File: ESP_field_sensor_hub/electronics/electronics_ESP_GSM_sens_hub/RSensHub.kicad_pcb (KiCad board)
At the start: 2 copper layers, 25 parts, among them J1 RJ45_Shielded, J2 RJ45_Shielded, J4 Conn_01x04_Female, Q1 IRF3205, Q2 IRF3205, Q3 IRF3205, Q4 IRF3205, Q5 IRF3205, Q6 IRF3205, U1 MAX48_module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

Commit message: Previous
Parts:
- added ANT: , myComponents:GNSSantennaVertical, F.Cu at (209.0, 26.7)
- added U4: SIM7000G_DEVBoard, myComponents:sim7000G_dev_board, F.Cu at (183.5, 45.7)
- moved U3 91.1 mm to (187.3, 106.0), turned to 90 degrees

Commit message: worked on sens hub PCB
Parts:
- removed ANT: , myComponents:GNSSantennaVertical
- added AE1: Antenna, myComponents:GNSSantennaVertical, F.Cu at (241.4, 30.5)
- added C2: 1000u16V, myComponents:CAP_Radial_D10.0mm_P5.00mm, F.Cu at (198.8, 38.7)
- added D1: LED, myComponents:LED_small_D3.0mm, F.Cu at (263.5, 50.2)
- added D2: LED, myComponents:LED_small_D3.0mm, F.Cu at (263.5, 60.3)
- added D4: LED, myComponents:LED_small_D3.0mm, F.Cu at (263.5, 65.4)
- added D5: LED, myComponents:LED_small_D3.0mm, F.Cu at (263.5, 70.5)
- added D6: LED, myComponents:LED_small_D3.0mm, F.Cu at (263.5, 45.1)
- added D7: LED, myComponents:LED_small_D3.0mm, F.Cu at (263.5, 55.2)
- added J6: Conn_01x04_Female, myComponents:TerminalBlockRemovablex4, F.Cu at (250.2, 90.8)
- added JP2: SolderJumper_2_Open, Jumper:SolderJumper-2_P1.3mm_Open_RoundedPad1.0x1.5mm, F.Cu at (217.8, 50.2)
- added JP3: Jumper_2_Bridged, myComponents:jumperx2_P2.54mm_widePads, F.Cu at (263.5, 77.5)
- added JP4: Jumper_2_Bridged, myComponents:jumperx2_P2.54mm_widePads, F.Cu at (263.5, 40.6)
- added JP5: Jumper_2_Bridged, myComponents:jumperx2_P2.54mm_widePads, F.Cu at (48.8, 16.8)
- added JP6: Jumper_2_Bridged, myComponents:jumperx2_P2.54mm_widePads, F.Cu at (52.3, 16.8)
- added R17: R, myComponents:resistor0.25,9mm, F.Cu at (248.3, 70.5)
- added R18: R, myComponents:resistor0.25,9mm, F.Cu at (248.2, 55.2)
- moved J1 147.2 mm to (232.4, 92.7), turned to 0 degrees
- moved U1 144.5 mm to (236.9, 37.5), turned to 270 degrees
- moved Q6 129.8 mm to (43.6, 89.2)
- moved R1 126.5 mm to (248.3, 50.2)
- moved J2 125.6 mm to (214.0, 92.7), turned to 0 degrees
- moved R2 125.0 mm to (248.3, 45.1)
- moved R15 118.8 mm to (33.0, 45.7)
- moved Q5 118.6 mm to (54.0, 78.9)
- moved R14 114.6 mm to (248.3, 65.4)
- moved R13 114.3 mm to (248.3, 60.3)
- moved J4 112.5 mm to (188.6, 90.2), turned to 90 degrees
- moved R16 100.6 mm to (50.8, 35.4)
- moved R3 98.0 mm to (38.8, 31.4)
- moved R12 86.7 mm to (63.6, 45.4)
- moved R9 86.2 mm to (64.8, 3.81)
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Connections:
- J2 pad 1: GND -> Net-(J2-Pad1)
- J2 pad 2: GND -> Net-(J2-Pad1)
- R1 pad 1: Net-(D1-Pad1) -> /SIM_IN_LED
- R1 pad 2: GND -> Net-(D1-Pad2)
- R13 pad 1: Net-(D4-Pad1) -> /COM_IN_LED
- R13 pad 2: GND -> Net-(D2-Pad2)
- R14 pad 1: Net-(D5-Pad1) -> /COM_OUT_LED
- R14 pad 2: GND -> Net-(D4-Pad2)
- R2 pad 1: Net-(D2-Pad1) -> /SIM_OUT_LED
- R2 pad 2: GND -> Net-(D6-Pad2)
- U1 pad 1: /UART2_RX -> /COM_IN_LED
- U1 pad 4: /UART2_TX -> /COM_OUT_LED
- U3 pad 14: Net-(U3-Pad14) -> GND
- U3 pad 19: Net-(U3-Pad19) -> +5V
- U3 pad 20: Net-(U3-Pad20) -> GND
- U3 pad 25: Net-(U3-Pad25) -> /UART2_DRIVER
- U3 pad 26: Net-(U3-Pad26) -> GND
- U3 pad 27: Net-(U3-Pad27) -> /COM_OUT_LED
- U3 pad 28: Net-(U3-Pad28) -> /COM_IN_LED
- U3 pad 30: Net-(U3-Pad30) -> /SIM_OUT_LED
- U3 pad 31: Net-(U3-Pad31) -> /SIM_IN_LED
- U4 pad 6: /uTX_SIM7000 -> /SIM_OUT_LED
- U4 pad 8: /uRX_SIM7000 -> /SIM_IN_LED

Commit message: short circuit protection - tested on dot board, ESP control pins not connected
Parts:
- removed D1, D2, D4, D5, D6, D7: LED, myComponents:LED_small_D3.0mm
- removed J6: Conn_01x04_Female, myComponents:TerminalBlockRemovablex4
- removed Q1, Q2, Q3, Q5, Q6: IRF3205, Package_TO_SOT_THT:TO-220-3_Vertical
- removed R1, R2: R, myComponents:resistor0.25,9mm
- removed R11, R15, R3: 470R, myComponents:resistor0.25,9mm
- removed R16, R7: 10K, myComponents:resistor0.25,9mm
- added C3: 100nF, myComponents:Capker_L4.6mm_W2.0mm_P2.50mm, F.Cu at (82.9, 68.1)
- added C4: 100nF, myComponents:Capker_L4.6mm_W2.0mm_P2.50mm, F.Cu at (82.9, 64.7)
- added JP1: SolderJumper_2_Open, Jumper:SolderJumper-2_P1.3mm_Open_RoundedPad1.0x1.5mm, F.Cu at (127.1, 77.7)
- added R19: 120, myComponents:resistor0.25,9mm, F.Cu at (86.7, 111.1)
- added R20: 120, myComponents:resistor0.25,9mm, F.Cu at (129.4, 91.8)
- added R21: 120, myComponents:resistor0.25,9mm, F.Cu at (156.0, 58.4)
- added R22: R, myComponents:resistor0.25,9mm, F.Cu at (110.8, 99.0)
- added R28: 1K, myComponents:resistor0.25,9mm, F.Cu at (232.0, 74.5)
- added R29: 1K, myComponents:resistor0.25,9mm, F.Cu at (86.7, 103.0)
- added R8: R0, myComponents:resistor0.25,9mm, F.Cu at (50.6, 110.3)
- added REF**: Box190x140x70, myComponents:Box190x140x70, F.Cu at (-521.5, -19.8)
- added RN1: R_Network08, myComponents:PinHeader_1x9_P2.54mm_widePads, F.Cu at (143.3, 32.6)
- added U10: PC817, myComponents:optoCouplerDIP4, F.Cu at (233.3, 78.2)
- added U11: PC817, myComponents:optoCouplerDIP4, F.Cu at (233.3, 84.3)
- added U12: PC817, myComponents:optoCouplerDIP4, F.Cu at (233.3, 68.6)
- added U2: 5V5ADCDC, myComponents:DCDC_HCW_P715, F.Cu at (29.8, 34.9)
- added U6: MULTICOL_LED_BAR, myComponents:DIP-20_LED_BAR_DISP, F.Cu at (131.3, 32.6)
- JP5: value Jumper_2_Bridged -> RS485 terminator
- JP6: value Jumper_2_Bridged -> SolderJumper_2_Open; footprint myComponents:jumperx2_P2.54mm_widePads -> Jumper:SolderJumper-2_P1.3mm_Open_RoundedPad1.0x1.5mm
- Q4: value IRF3205 -> IRF540N; footprint Package_TO_SOT_THT:TO-220-3_Vertical -> myComponents:TO-220-3_Horizontal_TabDown_bothSides
- R12: value 10K -> 330R
- R13, R18: value R -> 330R
- R14: value R -> 1K
- R17: value R -> 100K
- moved JP6 198.9 mm to (237.1, 90.3), turned to 90 degrees
- moved JP4 183.6 mm to (82.5, 71.4), turned to 0 degrees
- moved U4 181.5 mm to (27.0, 76.3)
- moved Q4 171.7 mm to (247.1, 84.8)
- moved R12 162.1 mm to (221.8, 80.9)
- moved U1 161.4 mm to (82.6, 85.0), turned to 0 degrees
- moved R18 148.0 mm to (104.5, 91.1)
- moved AE1 117.4 mm to (124.1, 33.1), turned to 0 degrees
- moved JP2 116.2 mm to (125.4, 120.5), turned to 0 degrees
- moved C2 109.6 mm to (112.8, 106.8), turned to 0 degrees
- moved R9 106.6 mm to (62.6, 110.3)
- moved JP3 103.3 mm to (170.8, 32.1), turned to 0 degrees
- moved R6 85.4 mm to (38.5, 110.3)
- moved R10 69.9 mm to (74.7, 110.3)
- moved R5 64.5 mm to (82.3, 99.0)
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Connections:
- J1 pad 1: GND -> /SAFE_BAT_GND
- J1 pad 2: GND -> /SAFE_BAT_GND
- J1 pad 7: VBUS -> +BATT
- J1 pad 8: VBUS -> +BATT
- J2 pad 1: Net-(J2-Pad1) -> /SAFE_BAT_GND
- J2 pad 2: Net-(J2-Pad1) -> /SAFE_BAT_GND
- J2 pad 7: VBUS -> +BATT
- J2 pad 8: VBUS -> +BATT
- J4 pad 2: /V_SOLAR -> +BATT
- J4 pad 4: +BATT -> /V_SOLAR
- JP3 pad 1: Net-(D2-Pad1) -> GND
- JP3 pad 2: GND -> Net-(JP3-Pad2)
- JP4 pad 1: Net-(D1-Pad1) -> GND
- JP4 pad 2: GND -> Net-(JP4-Pad2)
- JP5 pad 2: Net-(JP5-Pad2) -> /RS485_A
- Q4 pad 1: Net-(Q3-Pad1) -> Net-(JP6-Pad2)
- Q4 pad 2: /LOAD1_SOURCE -> /SAFE_BAT_GND
- R10 pad 2: /VREAD_ENABLED -> GND
- R12 pad 1: Net-(Q3-Pad1) -> GND
- R12 pad 2: GND -> Net-(R12-Pad2)
- R13 pad 1: /COM_IN_LED -> GND
- R14 pad 1: /COM_OUT_LED -> +BATT
- R17 pad 1: VBUS -> Net-(JP6-Pad1)
- R17 pad 2: Net-(D5-Pad2) -> GND
- R18 pad 1: +5V -> +3V3
- R6 pad 2: /VREAD_ENABLED -> GND

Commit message: worked on sens hub PCB layout, mostly done, needs finishing touches
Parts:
- removed the REF** at (-521.5, -19.8)
- added D3: D, myComponents:1N41_Diode, F.Cu at (306.7, 90.8)
- added J3: Conn_01x12_Male, myComponents:PinHeader_1x12_P2.54mm_widePads, F.Cu at (340.4, 83.2)
- added REF**: M3 mechanical, myComponents:M3 mechanical, F.Cu at (363.2, 26.7)
- added REF**: M3 mechanical, myComponents:M3 mechanical, F.Cu at (304.8, 77.9)
- added REF**: M3 mechanical, myComponents:M3 mechanical, F.Cu at (404.6, 77.9)
- added RV1: R_POT, myComponents:Potentiometer_ACP_CA9-V10_Vertical_Hole, F.Cu at (379.9, 100.9)
- JP1, JP2, JP6: moved to B.Cu
- moved JP4 319.5 mm to (400.1, 35.6)
- moved R29 319.1 mm to (404.0, 68.6), turned to 180 degrees
- moved U4 314.5 mm to (339.7, 43.2)
- moved R6 311.3 mm to (348.6, 83.2)
- moved R19 296.7 mm to (379.7, 64.7), turned to 270 degrees
- moved JP5 294.6 mm to (383.5, 76.8), turned to 270 degrees
- moved U1 294.2 mm to (372.1, 32.4), turned to 270 degrees
- moved U2 290.0 mm to (312.9, 97.8), turned to 90 degrees
- moved R22 286.1 mm to (391.2, 41.9), turned to 180 degrees
- moved R10 275.0 mm to (348.6, 87.0)
- moved C4 272.7 mm to (354.4, 90.2)
- moved C3 271.7 mm to (354.3, 80.0)
- moved U6 263.8 mm to (395.0, 41.9)
- moved RN1 263.3 mm to (406.4, 44.5)
- moved U3 256.5 mm to (345.4, 78.1)
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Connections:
- J4 pad 1: GND -> +BATT
- J4 pad 2: +BATT -> GND
- R5 pad 1: +BATT -> /V_SOLAR
- R9 pad 1: /V_SOLAR -> +BATT
- U3 pad 21: Net-(U3-Pad21) -> /Vout_OFF
- U3 pad 22: Net-(U3-Pad22) -> /Vout_ON
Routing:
- net GND: track 0.00 -> 408.1 mm
- net +5V: track 0.00 -> 251.3 mm, vias 0 -> 3
- net +BATT: track 0.00 -> 206.6 mm
- net /COM_IN_LED: track 0.00 -> 143.6 mm, vias 0 -> 6
- net /SIM_IN_LED: track 0.00 -> 136.9 mm, vias 0 -> 7
- net /SIM_OUT_LED: track 0.00 -> 133.6 mm, vias 0 -> 2
- net /COM_OUT_LED: track 0.00 -> 124.9 mm, vias 0 -> 6
- net /RS485_A: track 0.00 -> 115.0 mm
- net /RS485_B: track 0.00 -> 104.2 mm, vias 0 -> 9
- net /VN_PIN: track 0.00 -> 103.0 mm
- net Net-(JP6-Pad2): track 0.00 -> 81.5 mm
- net /VP_PIN: track 0.00 -> 78.0 mm
- net /UART2_DRIVER: track 0.00 -> 74.8 mm
- net /SAFE_BAT_GND: track 0.00 -> 65.3 mm
- net +3V3: track 0.00 -> 49.6 mm
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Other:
- board outline added: 116.8 x 107.3 mm

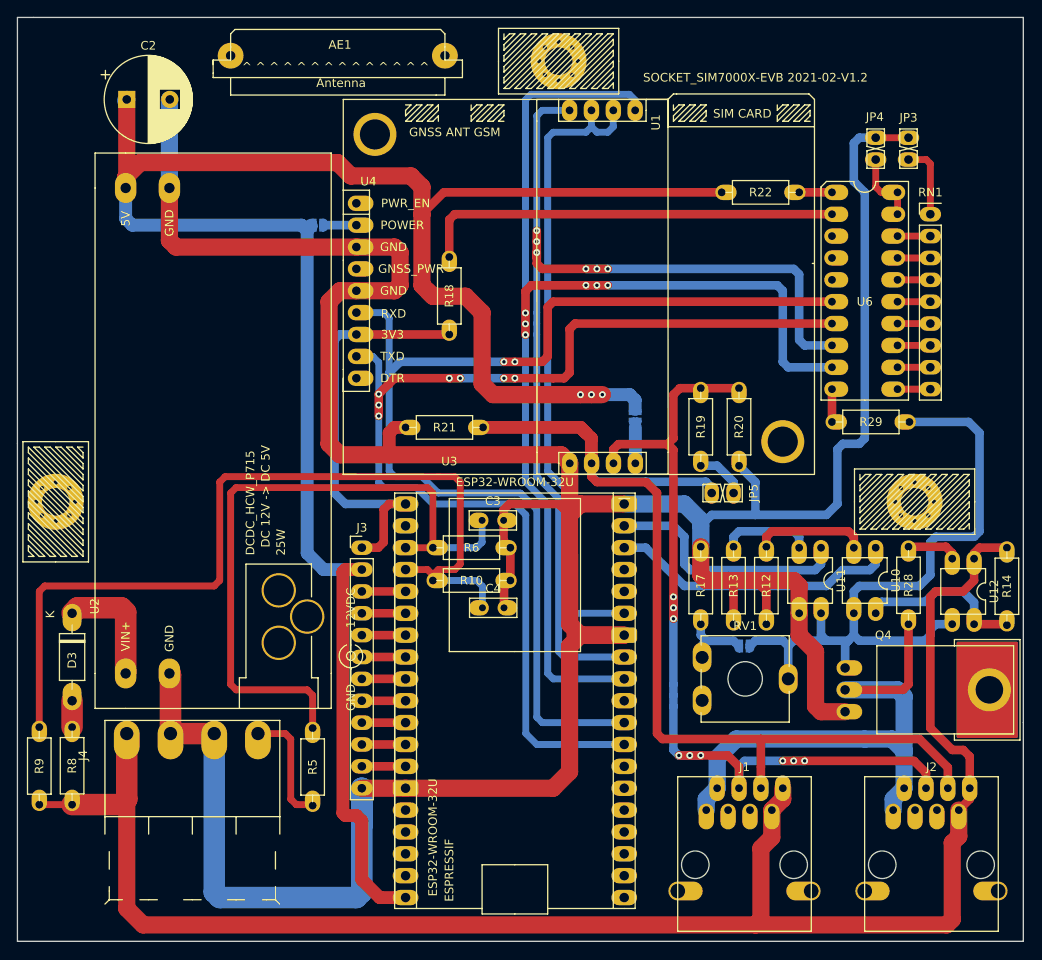
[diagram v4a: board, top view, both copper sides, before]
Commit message: routed and copper poutred PCB for ESP sensor hub TODO: labels and PCB logos
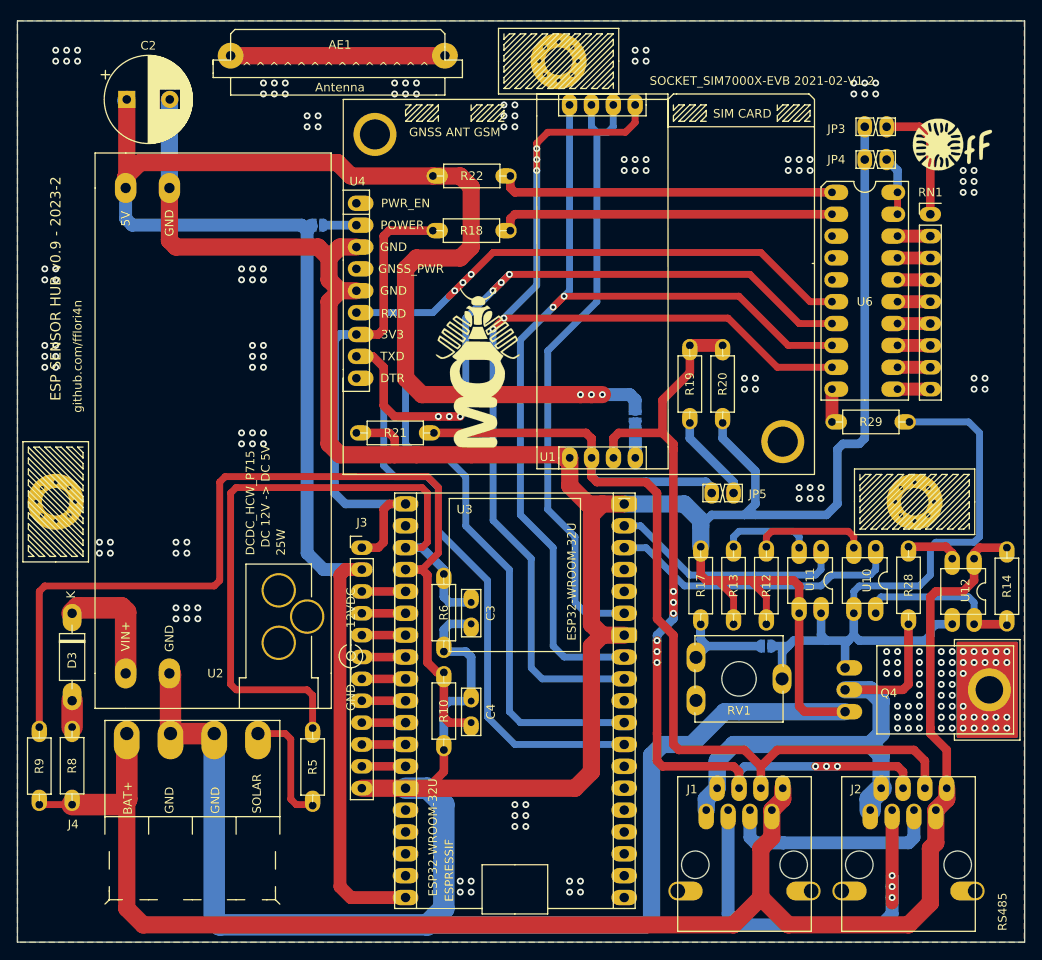
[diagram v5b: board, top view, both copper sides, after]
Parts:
- added G***: LOGO, myComponents:ma_Logo, F.Cu at (353.8, 62.2)
- added G***: LOGO, myComponents:xffLogo, B.Cu at (358.4, 115.8)
- added G***: LOGO, myComponents:xffLogo, F.Cu at (408.9, 36.3)
- moved R22 33.6 mm to (357.6, 40.0)
- moved C4 13.4 mm to (353.1, 103.5), turned to 90 degrees
- moved R18 12.2 mm to (348.6, 46.4), turned to 0 degrees
- moved R10 10.8 mm to (349.9, 97.7), turned to 270 degrees
- moved C3 9.61 mm to (353.1, 89.5), turned to 270 degrees
- moved R21 5.75 mm to (348.7, 69.8)
- moved R20 5.32 mm to (382.3, 59.7)
- moved JP3 5.24 mm to (398.8, 34.3), turned to 90 degrees
- moved R19 5.13 mm to (378.5, 59.7)
- moved R6 3.32 mm to (349.9, 86.2), turned to 270 degrees
- moved JP4 2.84 mm to (398.8, 38.1), turned to 90 degrees
- moved J2 2.67 mm to (399.4, 113.7)
- moved JP6 2.54 mm to (387.3, 94.6)
- moved RV1 0.71 mm to (379.2, 100.9)
- moved U1 0.63 mm to (372.1, 31.8)
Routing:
- net GND: track 408.1 -> 489.0 mm, vias 0 -> 126
- net /BUS_3: track 0.00 -> 47.4 mm, vias 0 -> 3
- net Net-(R22-Pad1): track 3.81 -> 39.0 mm
- net /BUS_5: track 0.00 -> 25.9 mm
- net Net-(AE1-Pad1): track 0.00 -> 24.9 mm
- net +5V: track 251.3 -> 231.7 mm
- net /SIM_IN_LED: track 136.9 -> 150.3 mm, vias 7 -> 6
- net /COM_OUT_LED: track 124.9 -> 112.7 mm, vias 6 -> 2
- net Net-(R18-Pad2): track 49.0 -> 39.0 mm
- net +3V3: track 49.6 -> 59.0 mm
- net /COM_IN_LED: track 143.6 -> 136.7 mm, vias 6 -> 5
- net /SAFE_BAT_GND: track 65.3 -> 58.4 mm
- net +BATT: track 206.6 -> 200.2 mm
- net /VN_PIN: track 103.0 -> 109.2 mm
- net Net-(JP3-Pad2): track 8.60 -> 14.5 mm
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- added copper zone on B.Cu, net GND
- added copper zone on F.Cu, net GND
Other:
- board size 116.8 x 107.3 mm -> 117 x 107 mm
- board text added: "BAT+"
- board text added: "ESP SENSOR HUB v0.9 - 2023-2"
- board text added: "GND"
- board text added: "RS485"
- board text added: "SOLAR"
- board text added: "github.com/fflori4n"
